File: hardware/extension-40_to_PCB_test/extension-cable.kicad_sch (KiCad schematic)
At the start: 55 parts, among them J1 XKTF-005, J2 Conn_01x08_Socket, U1 ED078KH6

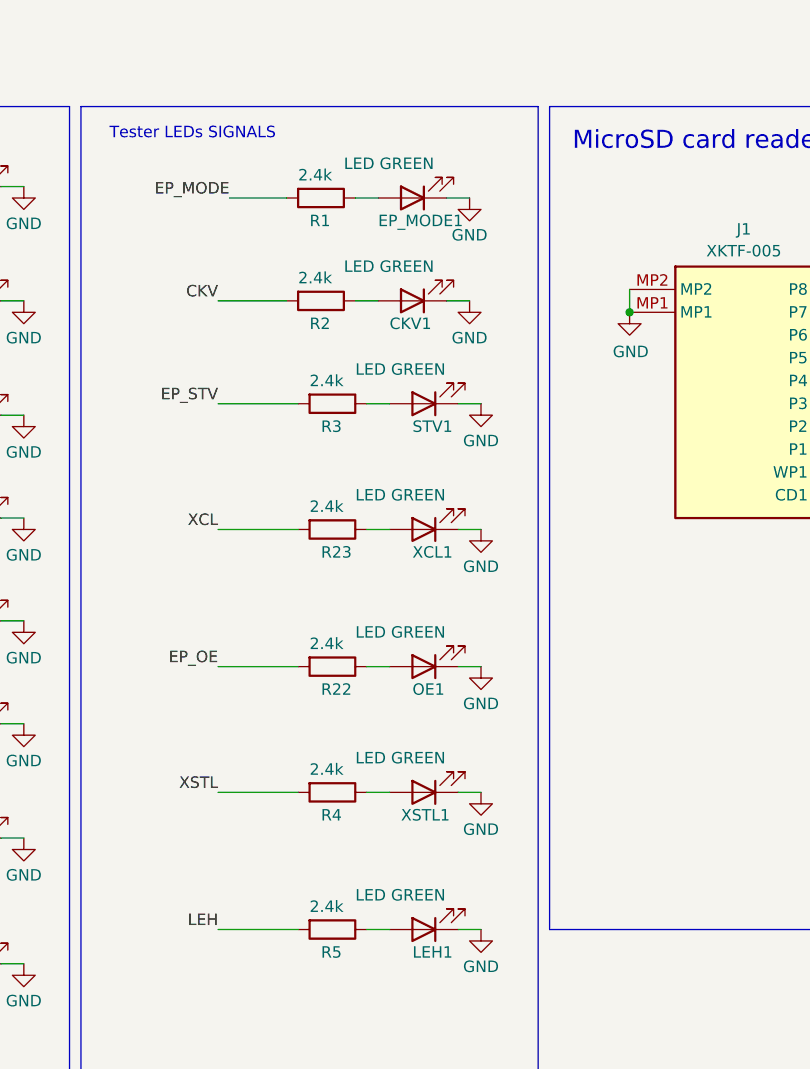
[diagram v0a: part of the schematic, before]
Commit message: 40 pin FPC tester sent to fabrication
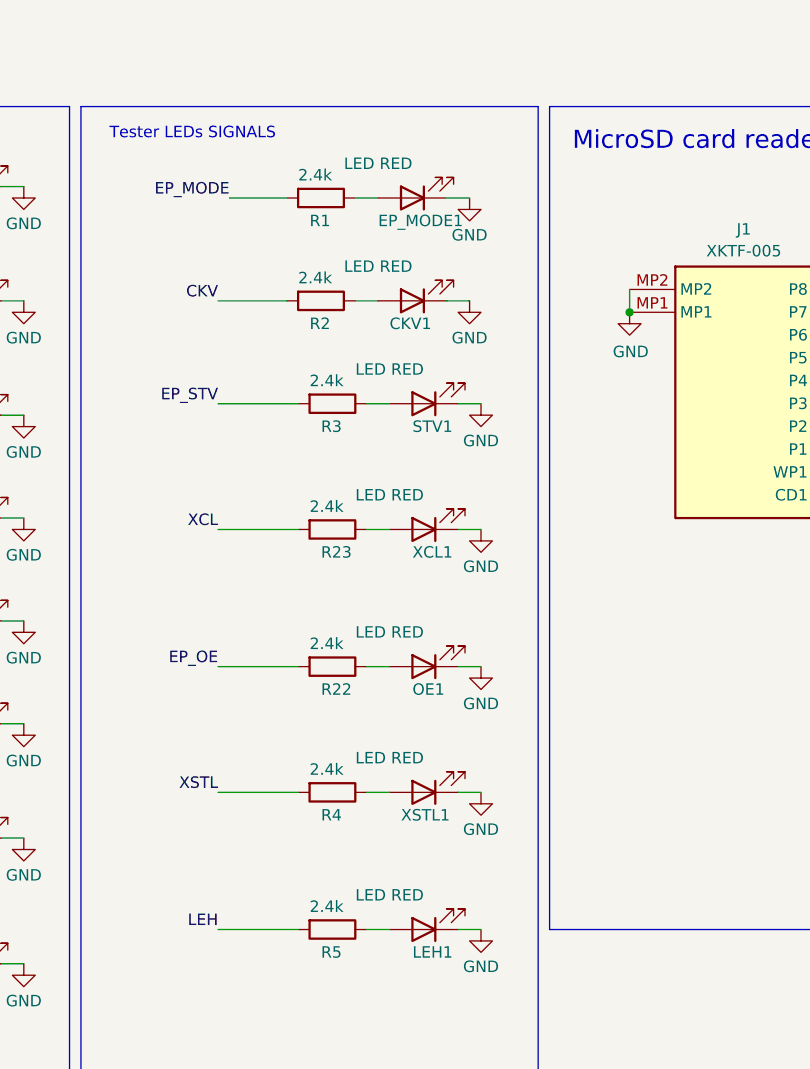
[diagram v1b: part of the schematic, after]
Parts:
- CKV1, EP_MODE1, LEH1, OE1, STV1, XCL1, XSTL1: value LED GREEN -> LED RED; LCSC C2297 -> C84256
- J2, TP1: now left out of the parts list
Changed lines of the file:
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@@
       (effects (font (size 1.27 1.27)) (justify right))
     )
-    (property "Value" "LED GREEN" (at 185.42 87.63 0)
+    (property "Value" "LED RED" (at 185.42 87.63 0)
       (effects (font (size 1.27 1.27)) (justify right))
     )
@@
       (effects (font (size 1.27 1.27)) hide)
     )
-    (property "LCSC" "C2297" (at 193.04 91.44 90)
+    (property "LCSC" "C84256" (at 193.04 91.44 90)
       (effects (font (size 1.27 1.27)) hide)
     )
@@
       (effects (font (size 1.27 1.27)) (justify right))
     )
-    (property "Value" "LED GREEN" (at 185.42 101.6 0)
+    (property "Value" "LED RED" (at 185.42 101.6 0)
       (effects (font (size 1.27 1.27)) (justify right))
     )
@@
       (effects (font (size 1.27 1.27)) hide)
     )
-    (property "LCSC" "C2297" (at 193.04 105.41 90)
+    (property "LCSC" "C84256" (at 193.04 105.41 90)
       (effects (font (size 1.27 1.27)) hide)
     )
@@
       (effects (font (size 1.27 1.27)) (justify right))
     )
-    (property "Value" "LED GREEN" (at 185.42 58.42 0)
+    (property "Value" "LED RED" (at 185.42 58.42 0)
       (effects (font (size 1.27 1.27)) (justify right))
     )
@@
       (effects (font (size 1.27 1.27)) hide)
     )
-    (property "LCSC" "C2297" (at 193.04 62.23 90)
+    (property "LCSC" "C84256" (at 193.04 62.23 90)
       (effects (font (size 1.27 1.27)) hide)
     )
@@
       (effects (font (size 1.27 1.27)) (justify right))
     )
-    (property "Value" "LED GREEN" (at 185.42 72.39 0)
+    (property "Value" "LED RED" (at 185.42 72.39 0)
       (effects (font (size 1.27 1.27)) (justify right))
     )
@@
       (effects (font (size 1.27 1.27)) hide)
     )
-    (property "LCSC" "C2297" (at 193.04 76.2 90)
+    (property "LCSC" "C84256" (at 193.04 76.2 90)
       (effects (font (size 1.27 1.27)) hide)
     )
@@
   )
   (symbol (lib_id "Connector:TestPoint") (at 43.18 138.43 0) (unit 1)
-    (in_bom yes) (on_board yes) (dnp no) (fields_autoplaced)
+    (in_bom no) (on_board yes) (dnp no) (fields_autoplaced)
     (property "Reference" "TP1" (at 44.577 133.9159 0)
       (effects (font (size 1.27 1.27)) (justify left))
@@
   )
   (symbol (lib_id "Connector:Conn_01x08_Socket") (at 255.27 105.41 180) (unit 1)
-    (in_bom yes) (on_board yes) (dnp no) (fields_autoplaced)
+    (in_bom no) (on_board yes) (dnp no) (fields_autoplaced)
     (property "Reference" "J2" (at 255.905 90.6485 0)
       (effects (font (size 1.27 1.27)))
@@
       (effects (font (size 1.27 1.27)) (justify right))
     )
-    (property "Value" "LED GREEN" (at 185.42 116.84 0)
+    (property "Value" "LED RED" (at 185.42 116.84 0)
       (effects (font (size 1.27 1.27)) (justify right))
     )
@@
       (effects (font (size 1.27 1.27)) hide)
     )
-    (property "LCSC" "C2297" (at 193.04 120.65 90)
+    (property "LCSC" "C84256" (at 193.04 120.65 90)
       (effects (font (size 1.27 1.27)) hide)
     )
@@
       (effects (font (size 1.27 1.27)) (justify right))
     )
-    (property "Value" "LED GREEN" (at 184.15 35.56 0)
+    (property "Value" "LED RED" (at 184.15 35.56 0)
       (effects (font (size 1.27 1.27)) (justify right))
     )
@@
       (effects (font (size 1.27 1.27)) hide)
     )
-    (property "LCSC" "C2297" (at 191.77 39.37 90)
+    (property "LCSC" "C84256" (at 191.77 39.37 90)
       (effects (font (size 1.27 1.27)) hide)
     )
@@
       (effects (font (size 1.27 1.27)) (justify right))
     )
-    (property "Value" "LED GREEN" (at 184.15 46.99 0)
+    (property "Value" "LED RED" (at 184.15 46.99 0)
       (effects (font (size 1.27 1.27)) (justify right))
     )
@@
       (effects (font (size 1.27 1.27)) hide)
     )
-    (property "LCSC" "C2297" (at 191.77 50.8 90)
-      (effects (font (size 1.27 1.27)) hide)
-    )
+    (property "LCSC" "C84256" (at 191.77 50.8 90)
+      (effects (font (size 1.27 1.27)) hide)
+    )
